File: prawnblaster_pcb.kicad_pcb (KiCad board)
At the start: 2 copper layers, 119.4 x 54.9 mm, 30 parts, among them J1 USB_B, J2 Conn_01x04, J3 Conn_Coaxial_x2, J4 Conn_Coaxial_x2, J5 Conn_Coaxial, J6 Conn_Coaxial, J7 Conn_01x02, U1 Pico, U2 ADuM5000, U3 ADUM4160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

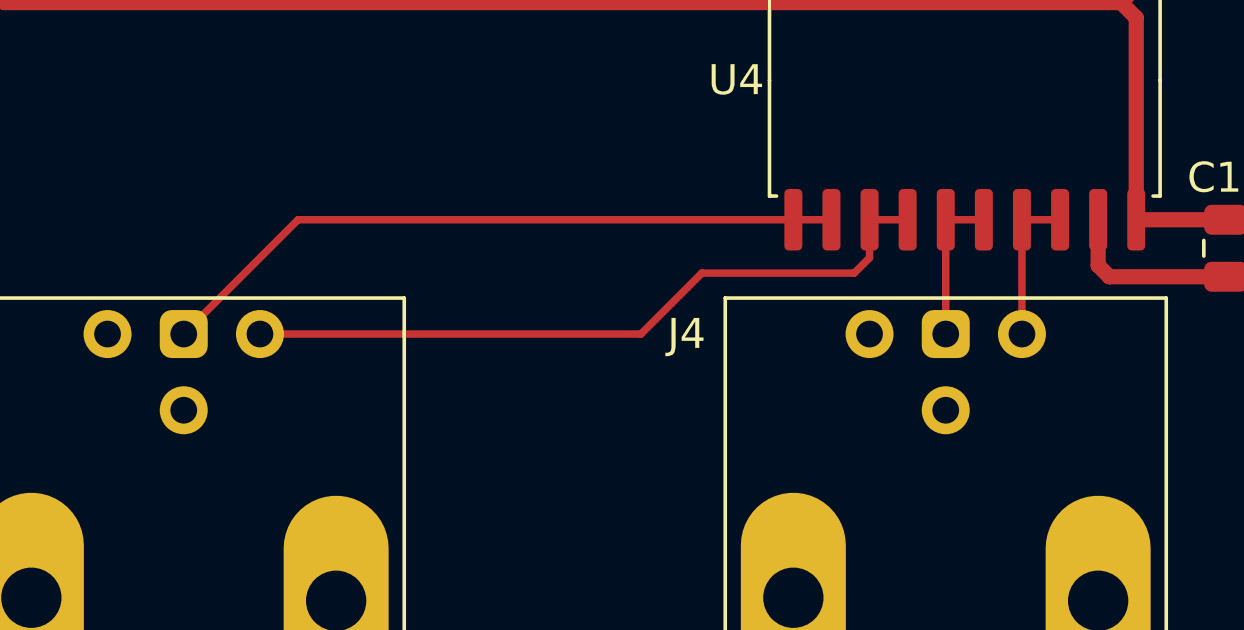
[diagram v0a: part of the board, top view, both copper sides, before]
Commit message: Fixed trigger plug wiring
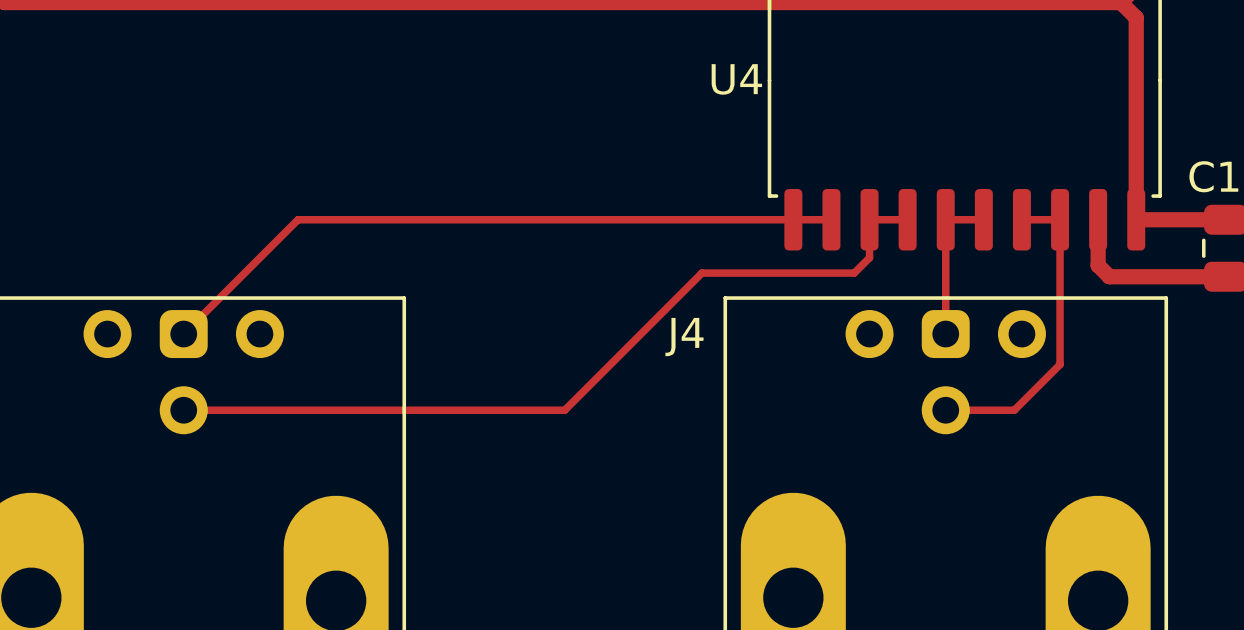
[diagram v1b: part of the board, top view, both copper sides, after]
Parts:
- J3: value Conn_Coaxial_x2 -> Clock01
- J4: value Conn_Coaxial_x2 -> Clock23
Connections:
- J3 pad 2: Net-(J3-Pad2) -> GND
- J3 pad 3: GND -> Net-(U4-Pad13)
- J3 pad 4: (no net) -> GND
- J4 pad 2: Net-(J4-Pad2) -> GND
- J4 pad 3: GND -> Net-(U4-Pad17)
- J4 pad 4: (no net) -> GND
- U4 pad 13: Net-(J3-Pad2) -> Net-(U4-Pad13)
- U4 pad 14: Net-(J3-Pad2) -> Net-(U4-Pad13)
- U4 pad 17: Net-(J4-Pad2) -> Net-(U4-Pad17)
- U4 pad 18: Net-(J4-Pad2) -> Net-(U4-Pad17)
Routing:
- net Net-(U4-Pad13): track 0.00 -> 27.5 mm
- net Net-(J3-Pad2): track 23.9 -> 0.00 mm
- net Net-(U4-Pad17): track 0.00 -> 10.5 mm
- net Net-(J4-Pad2): track 5.08 -> 0.00 mm

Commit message: Updated version number. Now 1.1
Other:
- board text added: "PrawnBlaster PCB v1.1 Designed by Carter T. in 2023"
- board text removed: "PrawnBlaster PCB v1 Designed by Carter T. in 2023"
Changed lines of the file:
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@@
     (effects (font (size 1 1) (thickness 0.15)) (justify mirror))
   )
-  (gr_text "PrawnBlaster PCB v1\nDesigned by Carter T. in 2023\n" (at 162.56 33.02) (layer "B.SilkS")
+  (gr_text "PrawnBlaster PCB v1.1\nDesigned by Carter T. in 2023\n" (at 162.56 33.02) (layer "B.SilkS")
     (effects (font (size 1 1) (thickness 0.15)) (justify mirror))
   )
@@
     (effects (font (size 1 1) (thickness 0.15)))
   )
-  (gr_text "PrawnBlaster PCB v1\nDesigned by Carter T. in 2023\n" (at 96.52 33.02) (layer "F.SilkS")
+  (gr_text "PrawnBlaster PCB v1.1\nDesigned by Carter T. in 2023\n" (at 96.52 33.02) (layer "F.SilkS")
     (effects (font (size 1 1) (thickness 0.15)))
   )
